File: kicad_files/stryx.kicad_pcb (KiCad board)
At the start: 2 copper layers, 57 x 85 mm, 26 parts, among them J1 Power, J2 Motor 2, J3 Motor 1, J4 USB_B_Micro, U1 LM317, U2 NUCLEO-L432KC, U3 HC-SR04, U4 TB6612FNG-Module, U5 NRF24L01_Breakout

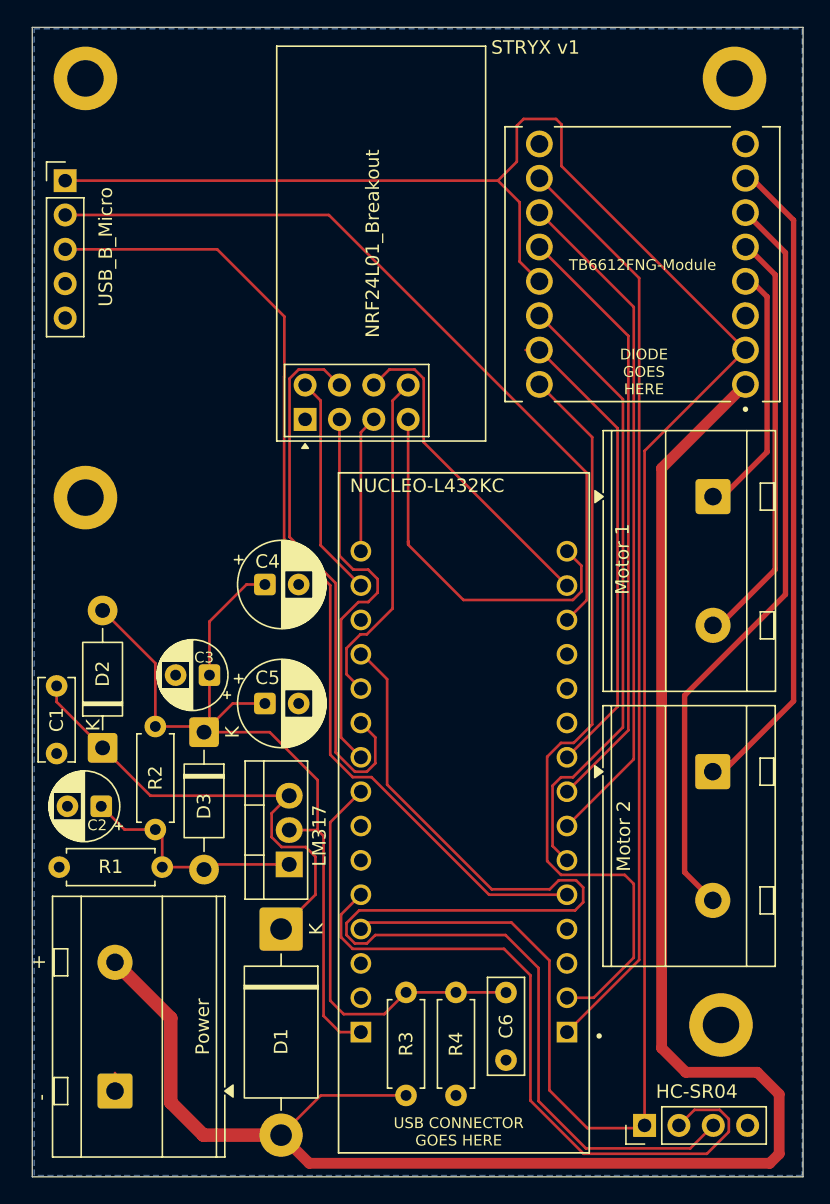
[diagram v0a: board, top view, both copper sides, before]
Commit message: fixed screw terminal footprint
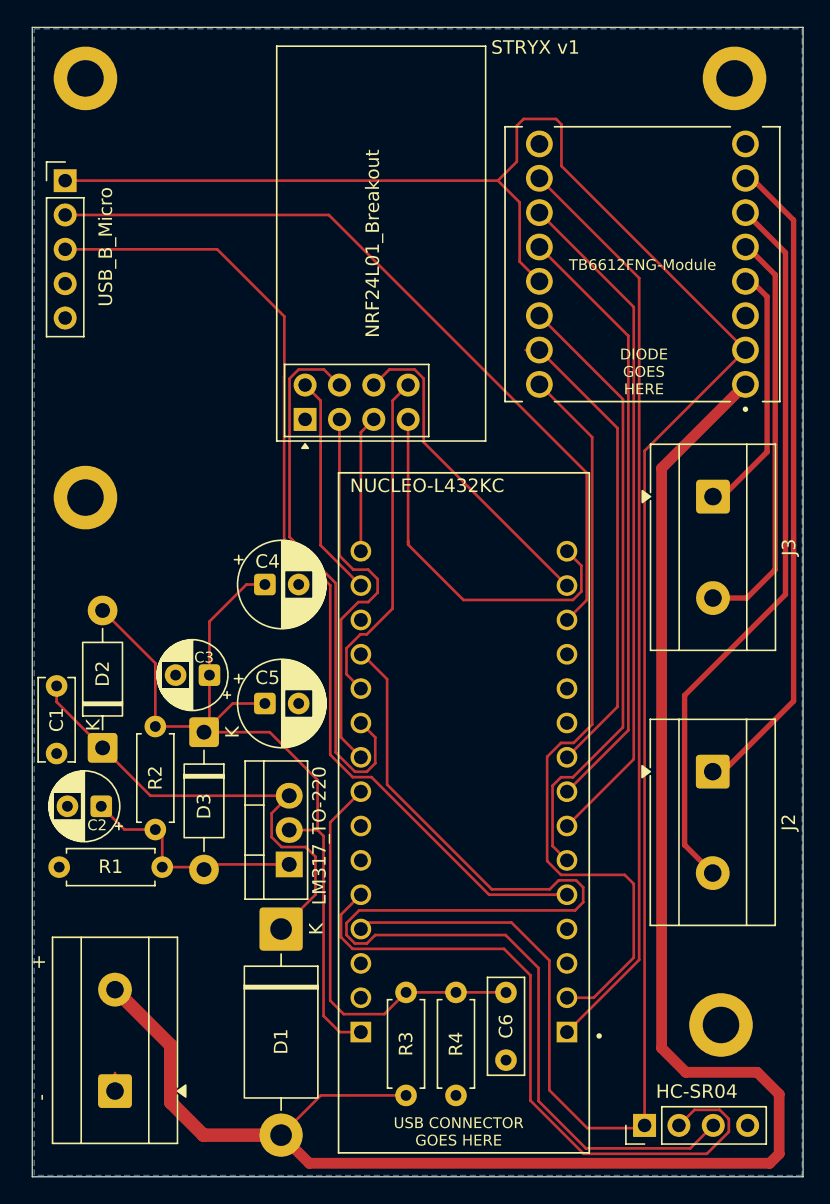
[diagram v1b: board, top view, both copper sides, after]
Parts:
- J1: value Power -> Screw_Terminal_Power; footprint TerminalBlock_MetzConnect:TerminalBlock_MetzConnect_Type703_RT10N02HGLU_1x02_P9.52mm_Horizontal -> TerminalBlock_MetzConnect:TerminalBlock_MetzConnect_Type171_RT13702HBWC_1x02_P7.50mm_Horizontal
- J2: value Motor 2 -> Screw_Terminal_M2; footprint TerminalBlock_MetzConnect:TerminalBlock_MetzConnect_Type703_RT10N02HGLU_1x02_P9.52mm_Horizontal -> TerminalBlock_MetzConnect:TerminalBlock_MetzConnect_Type171_RT13702HBWC_1x02_P7.50mm_Horizontal
- J3: value Motor 1 -> Screw_Terminal_M1; footprint TerminalBlock_MetzConnect:TerminalBlock_MetzConnect_Type703_RT10N02HGLU_1x02_P9.52mm_Horizontal -> TerminalBlock_MetzConnect:TerminalBlock_MetzConnect_Type171_RT13702HBWC_1x02_P7.50mm_Horizontal
- U1: value LM317 -> LM317_TO-220
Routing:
- net Vbat: track 135.8 -> 133.8 mm
- net Net-(J2-Pin_2): track 56.0 -> 54.0 mm
